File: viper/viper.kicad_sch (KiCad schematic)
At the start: 0 parts

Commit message: feat: switches and power
Signed-off-by: Matt Gleich <git@mattglei.ch>
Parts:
- added D1, D10, D11, D12, D2, D3, D4, D5, D6, D7, D8, D9: LED, symbol Device:LED
- added J1: Barrel_Jack, symbol Connector:Barrel_Jack
- added R1, R10, R11, R12, R2, R3, R4, R5, R6, R7, R8, R9: R_US, symbol Device:R_US
- added S1, S2, S3, S4, S5, S6: M2012SA1W03, M2012SA1W03, symbol M2012SA1W03:M2012SA1W03
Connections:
- new net: R1.2, S1.1 (ON)
- new net: D2.1 (K), R2.2
- new net: D1.2 (A), R1.1
- new net: D6.1 (K), R6.2
- new net: D8.2 (A), R9.1
- new net: R9.2, S5.1 (ON)
- new net: R3.2, S2.1 (ON)
- new net: D11.1 (K), R11.2
- new net: D10.2 (A), R10.1
- new net: R7.2, S4.1 (ON)
- new net: D4.1 (K), R4.2
- new net: D9.1 (K), R8.2
- new net: D7.2 (A), R7.1
- new net: D3.2 (A), R3.1
- new net: D12.1 (K), R12.2
- new net: R10.2, S6.1 (ON)
- new net: R5.2, S3.1 (ON)
- new net: D5.2 (A), R5.1
- new net GND: D1.1 (K), D10.1 (K), D11.2 (A), D12.2 (A), D2.2 (A), D3.1 (K), D4.2 (A), D5.1 (K), D6.2 (A), D7.1 (K), D8.1 (K), D9.2 (A), J1.1
- new net VBUS: J1.2, R11.1, R12.1, R2.1, R4.1, R6.1, R8.1, S1.2 (COM), S1.3 (ON), S2.2 (COM), S2.3 (ON), S3.2 (COM), S3.3 (ON), S4.2 (COM), S4.3 (ON), S5.2 (COM), S5.3 (ON), S6.2 (COM), S6.3 (ON)
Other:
- note added: "MARK I MASTER"
- note added: "MARK II MASTER"
- note added: "MARK III MASTER"
- note added: "MARK IV MASTER"
- note added: "MARK V MASTER"
- note added: "Switches & Power"
- note added: "VIPER MASTER"

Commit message: feat: pcbs and MARK I and MARK II
Signed-off-by: Matt Gleich <git@mattglei.ch>
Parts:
- added J2, J3, J4, J5, J6, J7, J8, J9: Conn_02x20_Odd_Even, symbol Connector_Generic:Conn_02x20_Odd_Even
- D1, D10, D11, D12, D2, D3, D4, D5, D6, D7, D8, D9: footprint (none) -> LED_THT:LED_D5.0mm
- J1: footprint (none) -> Connector_BarrelJack:BarrelJack_SwitchcraftConxall_RAPC10U_Horizontal
- R1, R10, R11, R12, R2, R3, R4, R5, R6, R7, R8, R9: footprint (none) -> Resistor_THT:R_Axial_DIN0207_L6.3mm_D2.5mm_P10.16mm_Horizontal
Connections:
- net GND: now also J2.6 (Pin_6), J3.6 (Pin_6), J4.6 (Pin_6), J5.6 (Pin_6), J6.6 (Pin_6), J7.6 (Pin_6), J8.6 (Pin_6), J9.6 (Pin_6)
- net VBUS: now also J2.4 (Pin_4), J3.4 (Pin_4), J4.2 (Pin_2), J5.2 (Pin_2), J6.2 (Pin_2), J7.2 (Pin_2), J8.4 (Pin_4), J9.4 (Pin_4)
- new net 3.3V: J2.1 (Pin_1), J3.1 (Pin_1), J4.1 (Pin_1), J5.1 (Pin_1)
- new net Chip Select: J2.24 (Pin_24), J3.24 (Pin_24), J6.24 (Pin_24), J7.24 (Pin_24)
- new net SCL: J2.5 (Pin_5), J3.5 (Pin_5), J4.5 (Pin_5), J5.5 (Pin_5)
- new net SDA: J2.3 (Pin_3), J3.3 (Pin_3), J4.3 (Pin_3), J5.3 (Pin_3)
- new net SPI0 MISO: J2.21 (Pin_21), J3.21 (Pin_21), J6.21 (Pin_21), J7.21 (Pin_21)
- new net SPI0 MOSI: J2.19 (Pin_19), J3.19 (Pin_19), J6.19 (Pin_19), J7.19 (Pin_19)
- new net SPI0 SCLK: J2.23 (Pin_23), J3.23 (Pin_23), J6.23 (Pin_23), J7.23 (Pin_23)
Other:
- note added: "MARK I"
- note added: "MARK II"

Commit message: feat: mark IV and V
Signed-off-by: Matt Gleich <git@mattglei.ch>
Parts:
- added Brd1: (no value), symbol SSD1306:SSD1306
- added D13, D14, D15, D16: LED, LED_THT:LED_D5.0mm, symbol Device:LED
- added J10, J12, J?: Conn_01x04_Male, symbol Connector:Conn_01x04_Male
- added J11: Conn_01x05_Male, symbol Connector:Conn_01x05_Male
- added R13, R14, R15, R16: R_US, Resistor_THT:R_Axial_DIN0207_L6.3mm_D2.5mm_P10.16mm_Horizontal, symbol Device:R_US
- added S7, S8: M2012SA1W03, M2012SA1W03:M2012SA1W03, symbol M2012SA1W03:M2012SA1W03
- added U1, U2, U?: Pico, RPi_Pico:RPi_Pico_SMD_TH, symbol MCU_RaspberryPi_and_Boards:Pico
- J2, J3, J4, J5, J6, J7, J8, J9: footprint (none) -> Connector_PinHeader_2.00mm:PinHeader_2x20_P2.00mm_Vertical
- S1, S2, S3, S4, S5, S6: footprint M2012SA1W03 -> M2012SA1W03:M2012SA1W03
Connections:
- net GND: now also D12.1 (K), D13.2 (A), D14.2 (A), D15.1 (K), D16.2 (A), U1.3 (GND), U1.42 (GND), U2.3 (GND), U2.42 (GND), U?.3 (GND), U?.42 (GND); no longer D12.2 (A)
- net VBUS: now also Brd1.2 (VCC), J11.4 (Pin_4), J11.5 (Pin_5), R14.1, R16.1, S7.2 (COM), S7.3 (ON), S8.2 (COM), S8.3 (ON), U1.40 (VBUS), U2.40 (VBUS), U?.40 (VBUS); no longer J1.2, S5.2 (COM)
- net at R12.2: now also D13.1 (K); no longer D12.1 (K)
- new net: D14.1 (K), R14.2
- new net: D15.2 (A), R15.1
- new net: R15.2, S8.1 (ON)
- new net: J12.1 (Pin_1), U2.1 (GPIO0)
- new net: J12.2 (Pin_2), U2.2 (GPIO1)
- new net: J12.3 (Pin_3), U2.41 (SWCLK)
- new net: J12.4 (Pin_4), U2.43 (SWDIO)
- new net: J?.1 (Pin_1), U?.1 (GPIO0)
- new net: J?.2 (Pin_2), U?.2 (GPIO1)
- new net: J?.3 (Pin_3), U?.41 (SWCLK)
- new net: J?.4 (Pin_4), U?.43 (SWDIO)
- new net: D16.1 (K), R16.2
- new net: J1.2, S5.2 (COM)
- new net: D12.2 (A), R13.1
- new net: J10.1 (Pin_1), U1.1 (GPIO0)
- new net: J10.2 (Pin_2), U1.2 (GPIO1)
- new net: J11.2 (Pin_2), U1.21 (GPIO16)
- new net: J11.1 (Pin_1), U1.22 (GPIO17)
- new net: J11.3 (Pin_3), U1.38 (GND)
- new net: J10.3 (Pin_3), U1.41 (SWCLK)
- new net: J10.4 (Pin_4), U1.43 (SWDIO)
- new net: Brd1.3 (SCL), U2.21 (GPIO16)
- new net: Brd1.4 (SDA), U2.22 (GPIO17)
- new net: Brd1.1 (GND), U2.38 (GND)
- new net: R13.2, S7.1 (ON)
- no-connect marks 0 -> 375
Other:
- note added: "DEBUG ROUTE"
- note added: "MARK DEBUG MASTER"
- note added: "MARK IV"
- note added: "MARK V"

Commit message: feat: assign footprints
verification still needed

Signed-off-by: Matt Gleich <git@mattglei.ch>
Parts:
- removed D15, D16: LED, LED_THT:LED_D5.0mm, symbol Device:LED
- removed J10, J12, J?: Conn_01x04_Male, symbol Connector:Conn_01x04_Male
- removed J7, J8: Conn_02x20_Odd_Even, Connector_PinHeader_2.00mm:PinHeader_2x20_P2.00mm_Vertical, symbol Connector_Generic:Conn_02x20_Odd_Even
- removed R15, R16: R_US, Resistor_THT:R_Axial_DIN0207_L6.3mm_D2.5mm_P10.16mm_Horizontal, symbol Device:R_US
- removed S8: M2012SA1W03, M2012SA1W03:M2012SA1W03, symbol M2012SA1W03:M2012SA1W03
- added Brd2, Brd3: SSD1306, symbol SSD1306:SSD1306
- added J10, J7: DEBUG PINS, symbol Connector_Generic:Conn_02x02_Counter_Clockwise
- added J12, J13: (no value), Connector_PinHeader_2.00mm:PinHeader_2x20_P2.00mm_Vertical, symbol Connector_Generic:Conn_02x20_Odd_Even
- added J8: DEBUG Pins, symbol Connector_Generic:Conn_02x02_Counter_Clockwise
- Brd1: value (none) -> SSD1306; footprint (none) -> SSD1306:128x64OLED
- J1: footprint Connector_BarrelJack:BarrelJack_SwitchcraftConxall_RAPC10U_Horizontal -> (none)
- J2, J4, J6: value Conn_02x20_Odd_Even -> (none)
- J3, J5, J9: value Conn_02x20_Odd_Even -> RPI Headers
- gave numbers to parts that had none: 1
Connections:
- net Chip Select: no longer J2.24 (Pin_24), J6.24 (Pin_24)
- net GND: now also Brd2.1 (GND), Brd3.1 (GND), J12.6 (Pin_6), J13.6 (Pin_6)
- net SPI0 MISO: no longer J2.21 (Pin_21), J6.21 (Pin_21)
- net SPI0 MOSI: no longer J2.19 (Pin_19), J6.19 (Pin_19)
- net SPI0 SCLK: no longer J2.23 (Pin_23), J6.23 (Pin_23)
- net VBUS: now also J6.4 (Pin_4), Brd2.2 (VCC), Brd3.2 (VCC), J12.2 (Pin_2), J12.4 (Pin_4), J13.2 (Pin_2), J13.4 (Pin_4)
- net at U2.1 (GPIO0): now also J7.4 (Pin_4)
- net at U2.2 (GPIO1): now also J7.3 (Pin_3)
- net at U2.41 (SWCLK): now also J7.2 (Pin_2)
- net at U2.43 (SWDIO): now also J7.1 (Pin_1)
- net at U3.1 (GPIO0): now also J8.4 (Pin_4)
- net at U3.2 (GPIO1): now also J8.3 (Pin_3)
- net at U3.41 (SWCLK): now also J8.2 (Pin_2)
- net at U3.43 (SWDIO): now also J8.1 (Pin_1)
- net at U1.1 (GPIO0): now also J10.4 (Pin_4)
- net at U1.2 (GPIO1): now also J10.3 (Pin_3)
- net at U1.41 (SWCLK): now also J10.2 (Pin_2)
- net at U1.43 (SWDIO): now also J10.1 (Pin_1)
- net GPIO 5: now reaches J6.16 (Pin_16)
- net GPIO 5: now also J2.29 (Pin_29)
- net GPIO 6: now reaches J6.18 (Pin_18)
- net GPIO 6: now also J2.31 (Pin_31)
- net SDA 02: now reaches J3.27 (Pin_27)
- net SDA 02: now also J2.27 (Pin_27), Brd2.4 (SDA), Brd3.4 (SDA)
- net SCL 02: now reaches J3.28 (Pin_28)
- net SCL 02: now also J2.28 (Pin_28), Brd2.3 (SCL), Brd3.3 (SCL)
- net GPIO 27: now reaches J2.13 (Pin_13)
- net GPIO 27: now also J13.16 (Pin_16)
- net GPIO 22: now reaches J2.15 (Pin_15)
- net GPIO 22: now also J13.18 (Pin_18)
- net GPIO 23: now reaches J2.16 (Pin_16)
- net GPIO 23: now also J12.16 (Pin_16)
- net GPIO 24: now reaches J2.18 (Pin_18)
- net GPIO 24: now also J12.18 (Pin_18)
- net SCL renamed SCL 01
- net SDA renamed SDA 01
- no-connect marks 375 -> 371
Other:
- note added: "Adafruit CharliePlex Bonnet"
- note added: "Raspberry Pi Zero W2"
- note added: "Waveshare EINK Display"
- note removed: "DEBUG ROUTE"
- moved on the sheet: Brd1, D1, D10, D11, D12, D13, D14, D2, D3, D4, D5, D6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

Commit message: chore: align items on board
Signed-off-by: Matt Gleich <git@mattglei.ch>
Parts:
- removed D12, D14: LED, LED_THT:LED_D5.0mm, symbol Device:LED
- removed R13, R14: R_US, Resistor_THT:R_Axial_DIN0207_L6.3mm_D2.5mm_P10.16mm_Horizontal, symbol Device:R_US
- removed S7: M2012SA1W03, M2012SA1W03:M2012SA1W03, symbol M2012SA1W03:M2012SA1W03
- Brd2, Brd3: footprint (none) -> SSD1306:128x64OLED
- J1: footprint (none) -> Connector_BarrelJack:BarrelJack_Wuerth_6941xx301002
- J10, J7, J8: footprint (none) -> Connector_PinHeader_2.00mm:PinHeader_2x02_P2.00mm_Vertical
- J11: footprint (none) -> Connector_PinHeader_2.00mm:PinHeader_1x05_P2.00mm_Vertical
- J12, J13, J6: value (none) -> Pimoroni BLINKT!
- J2: value (none) -> Raspberry Pi Zero W2
- J4: value (none) -> Adafruit CharliePlex Bonnet
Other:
- note removed: "MARK DEBUG MASTER"
- moved on the sheet: Brd1, J10, J11, J7, J8, U1, U2, U3

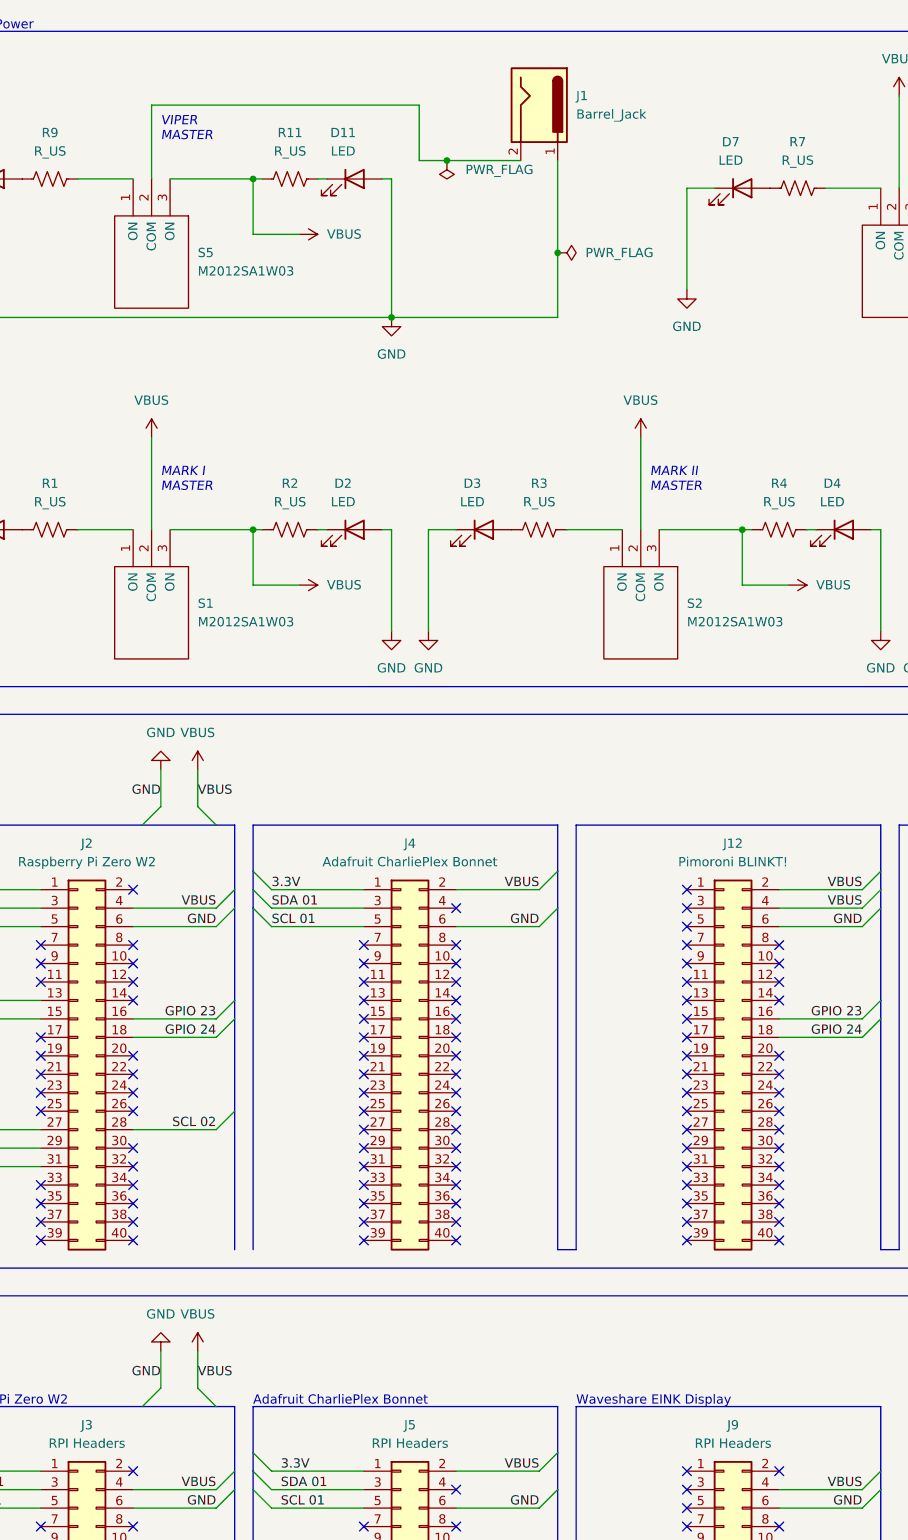
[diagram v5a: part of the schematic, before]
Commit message: feat: correct footprints and start PCB
Signed-off-by: Matt Gleich <git@mattglei.ch>
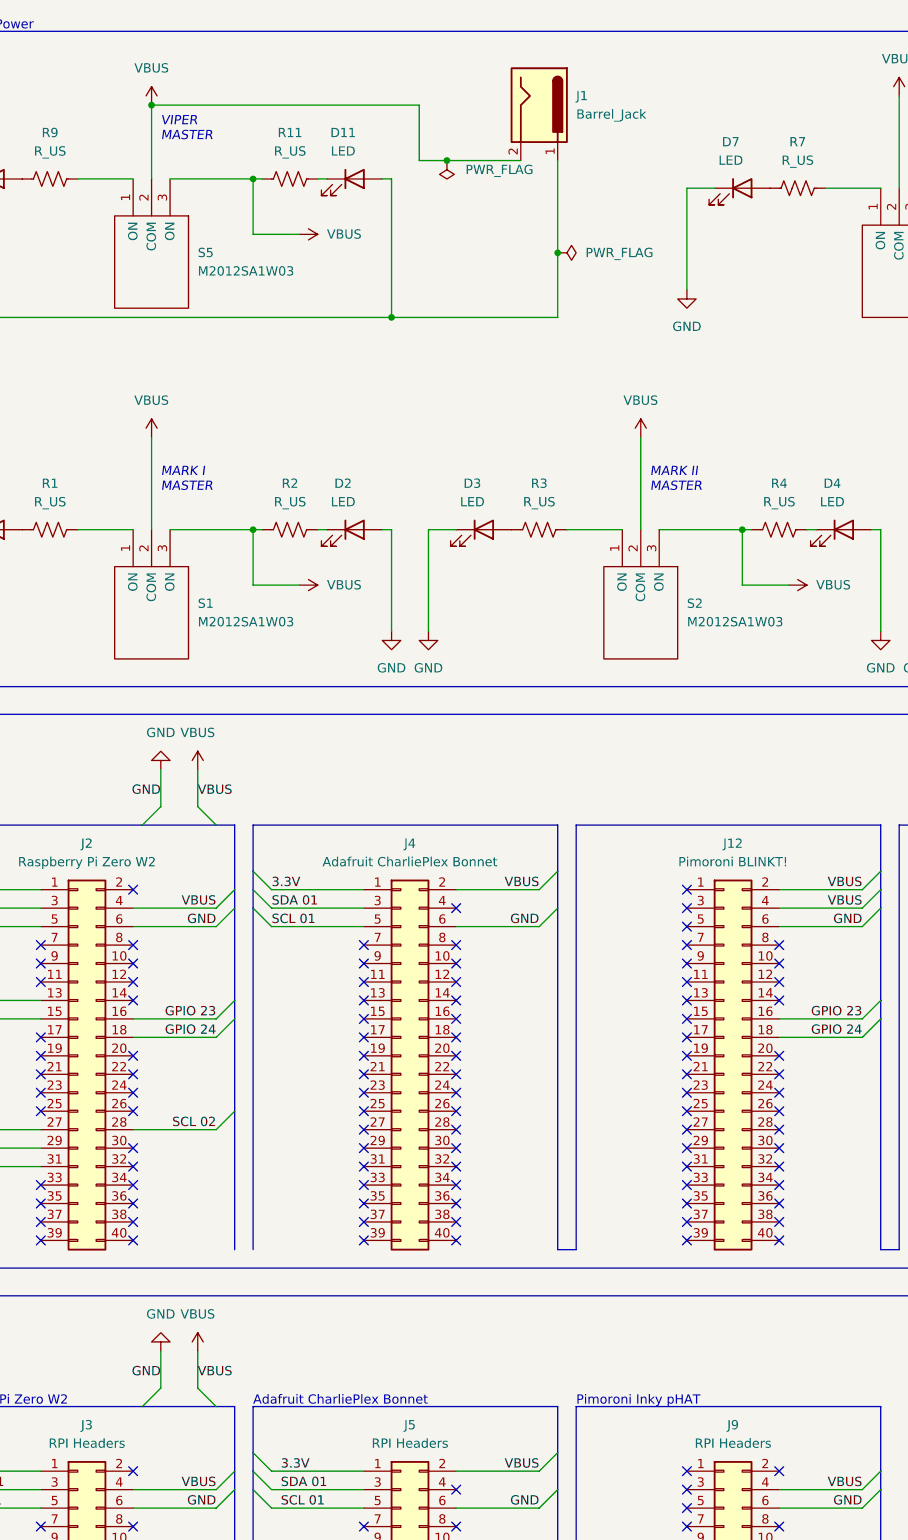
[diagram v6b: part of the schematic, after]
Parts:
- J10, J7, J8: footprint Connector_PinHeader_2.00mm:PinHeader_2x02_P2.00mm_Vertical -> (none)
- J11: footprint Connector_PinHeader_2.00mm:PinHeader_1x05_P2.00mm_Vertical -> (none)
- J12, J13, J2, J3, J4, J5, J6, J9: footprint Connector_PinHeader_2.00mm:PinHeader_2x20_P2.00mm_Vertical -> (none)
- U1, U2, U3: footprint RPi_Pico:RPi_Pico_SMD_TH -> Pico:RPi_Pico_SMD_TH
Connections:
- net VBUS: now also J1.2, S5.2 (COM)
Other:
- note added: "Pimoroni Inky pHAT"
- note removed: "Waveshare EINK Display"

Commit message: feat: off switch routing
Signed-off-by: Matt Gleich <git@mattglei.ch>
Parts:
- Brd1, Brd2, Brd3: value SSD1306 -> (none); footprint SSD1306:128x64OLED -> (none)
- D1, D10, D11, D13, D2, D3, D4, D5, D6, D7, D8, D9: value LED -> (none); footprint LED_THT:LED_D5.0mm -> (none)
- J1: value Barrel_Jack -> (none); footprint Connector_BarrelJack:BarrelJack_Wuerth_6941xx301002 -> (none)
- J10, J7: value DEBUG PINS -> (none)
- J11: value Conn_01x05_Male -> (none)
- J12, J13, J6: value Pimoroni BLINKT! -> (none)
- J2: value Raspberry Pi Zero W2 -> (none)
- J3, J5, J9: value RPI Headers -> (none)
- J4: value Adafruit CharliePlex Bonnet -> (none)
- J8: value DEBUG Pins -> (none)
- R1, R10, R11, R12, R2, R3, R4, R5, R6, R7, R8, R9: value R_US -> (none); footprint Resistor_THT:R_Axial_DIN0207_L6.3mm_D2.5mm_P10.16mm_Horizontal -> (none)
- S1, S2, S3, S4, S5, S6: value M2012SA1W03 -> (none); footprint M2012SA1W03:M2012SA1W03 -> (none)
- U1, U2, U3: value Pico -> (none); footprint Pico:RPi_Pico_SMD_TH -> (none)
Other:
- note removed: "MARK I MASTER"
- note removed: "MARK II MASTER"
- note removed: "MARK III MASTER"
- note removed: "MARK IV MASTER"
- note removed: "MARK V MASTER"
- note removed: "VIPER MASTER"

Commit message: feat: improve arrangement
Signed-off-by: Matt Gleich <git@mattglei.ch>
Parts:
- added J14: (no value), symbol Connector_Generic:Conn_02x20_Odd_Even
- Brd1, Brd2, Brd3: value (none) -> SSD1306; footprint (none) -> SSD1306:128x64OLED
- D1, D10, D11, D13, D2, D3, D4, D5, D6, D7, D8, D9: value (none) -> LED; footprint (none) -> LED_THT:LED_D5.0mm
- J1: value (none) -> Barrel_Jack; footprint (none) -> Connector_BarrelJack:BarrelJack_Wuerth_6941xx301002
- J10, J7: value (none) -> DEBUG PINS; footprint (none) -> Connector_PinHeader_2.54mm:PinHeader_2x02_P2.54mm_Vertical
- J11: value (none) -> Conn_01x05_Male
- J12, J13, J6: value (none) -> Pimoroni BLINKT!; footprint (none) -> Connector_PinHeader_2.54mm:PinHeader_2x20_P2.54mm_Vertical
- J2, J3: value (none) -> Raspberry Pi Zero W2; footprint (none) -> Connector_PinHeader_2.54mm:PinHeader_2x20_P2.54mm_Vertical
- J4, J5: value (none) -> Adafruit CharliePlex Bonnet; footprint (none) -> Connector_PinHeader_2.54mm:PinHeader_2x20_P2.54mm_Vertical
- J8: value (none) -> DEBUG Pins; footprint (none) -> Connector_PinHeader_2.54mm:PinHeader_2x02_P2.54mm_Vertical
- J9: value (none) -> Pimoroni Inky pHAT; footprint (none) -> Connector_PinHeader_2.54mm:PinHeader_2x20_P2.54mm_Vertical
- R1, R10, R11, R12, R2, R3, R4, R5, R6, R7, R8, R9: value (none) -> 330Ω; footprint (none) -> Resistor_THT:R_Axial_DIN0207_L6.3mm_D2.5mm_P10.16mm_Horizontal
- S1: value (none) -> MARK I; footprint (none) -> M2012SA1W03:M2012SA1W03
- S2: value (none) -> MARK II; footprint (none) -> M2012SA1W03:M2012SA1W03
- S3: value (none) -> MARK III; footprint (none) -> M2012SA1W03:M2012SA1W03
- S4: value (none) -> MARK IV; footprint (none) -> M2012SA1W03:M2012SA1W03
- S5: value (none) -> MASTER; footprint (none) -> M2012SA1W03:M2012SA1W03
- S6: value (none) -> MARK V; footprint (none) -> M2012SA1W03:M2012SA1W03
- U1, U2, U3: value (none) -> Pico; footprint (none) -> Pico:RPi_Pico_SMD_TH
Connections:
- net VBUS: now also J14.2 (Pin_2)
- net at U3.21 (GPIO16): now also J14.5 (Pin_5)
- net at U3.22 (GPIO17): now also J14.3 (Pin_3)
- net at U3.37 (3V3_EN): now also J14.1 (Pin_1)
- net at U3.38 (GND): now also J14.6 (Pin_6)
- no-connect marks 371 -> 402
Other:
- note removed: "Adafruit CharliePlex Bonnet"
- note removed: "Pimoroni Inky pHAT"
- note removed: "Raspberry Pi Zero W2"
- moved on the sheet: J8, U3
